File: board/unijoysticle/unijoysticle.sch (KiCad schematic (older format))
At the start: 14 parts, among them IC1 7405, IC2 7405, J1 DB9_Female, J2 DB9_Female, J3 Barrel_Jack, SW1 SW_Push, SW2 SW_SPST

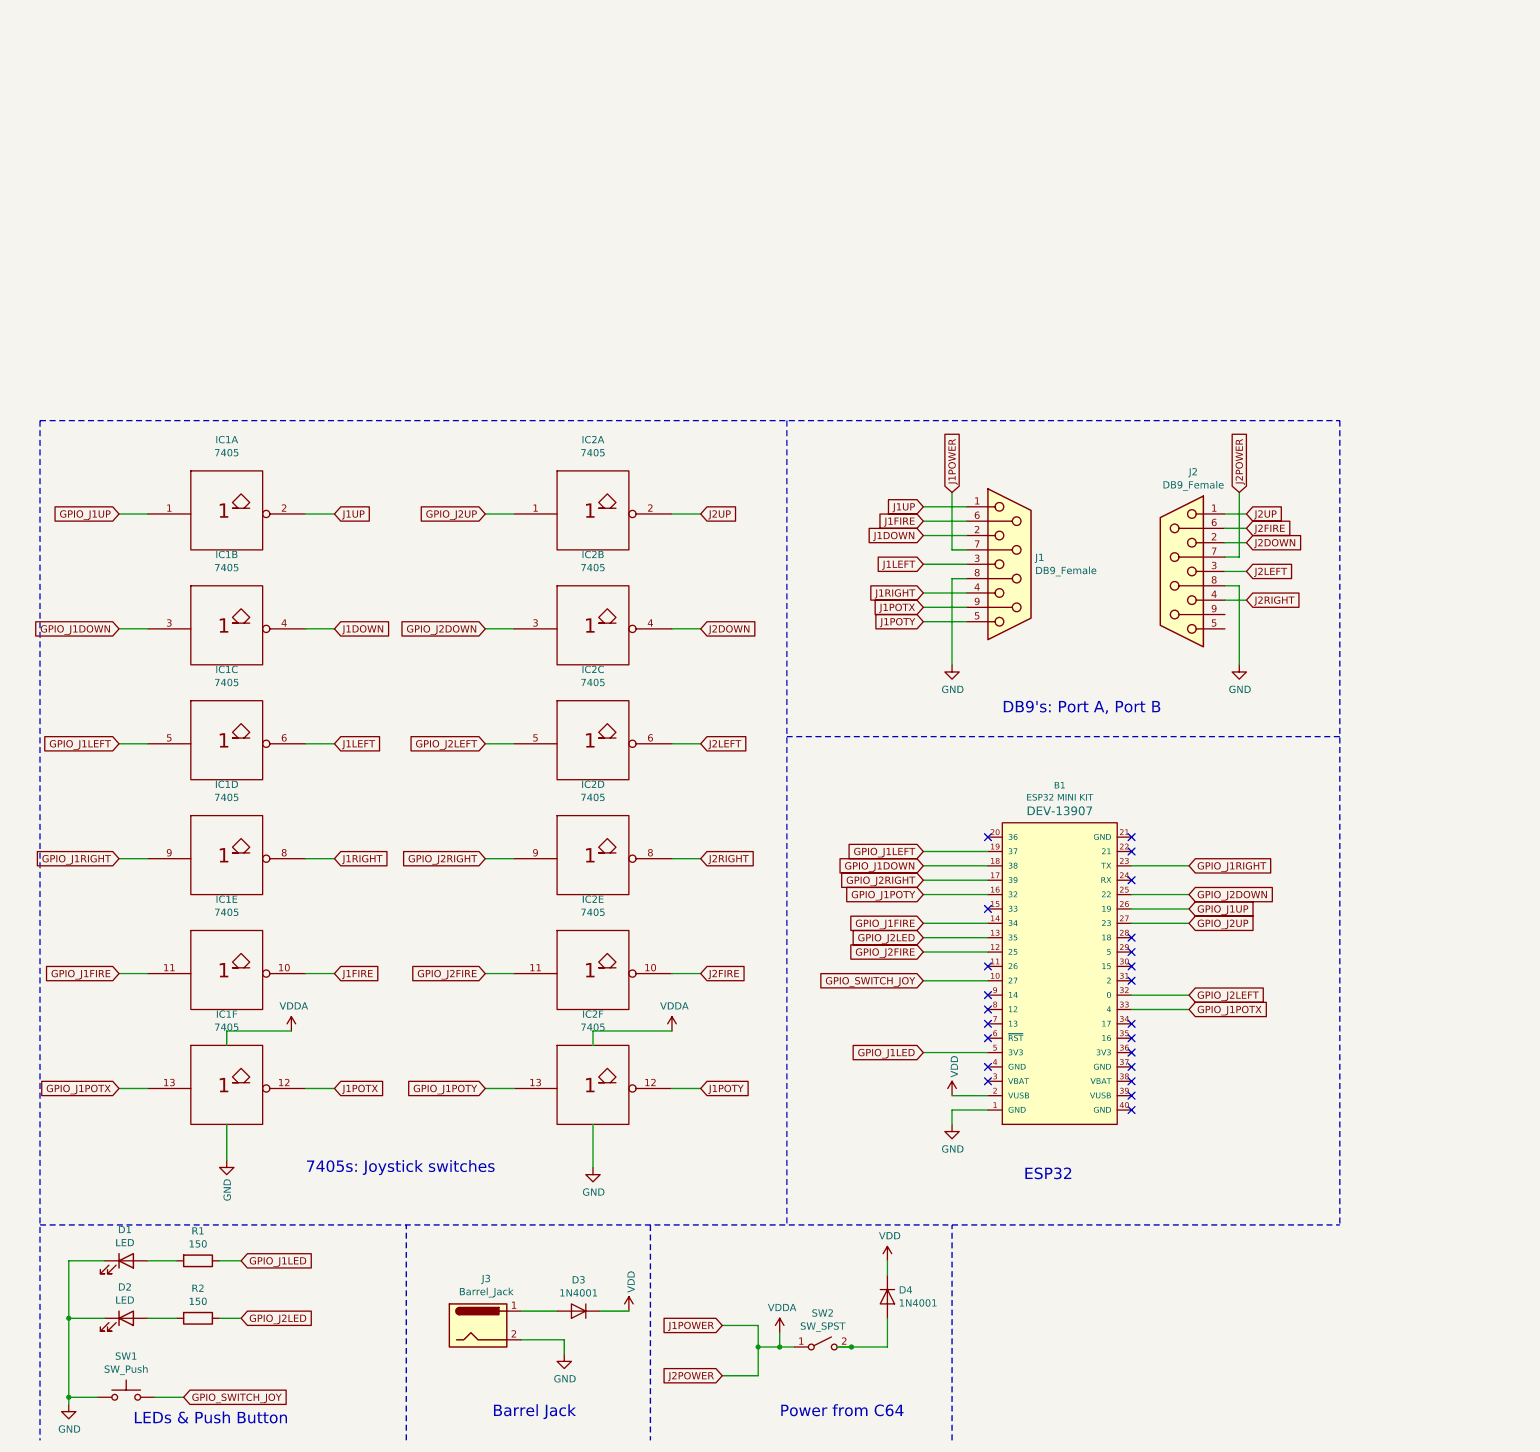
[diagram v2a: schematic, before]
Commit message: layout / schematic: replaced 7405 model with one with comes with pwr/gnd
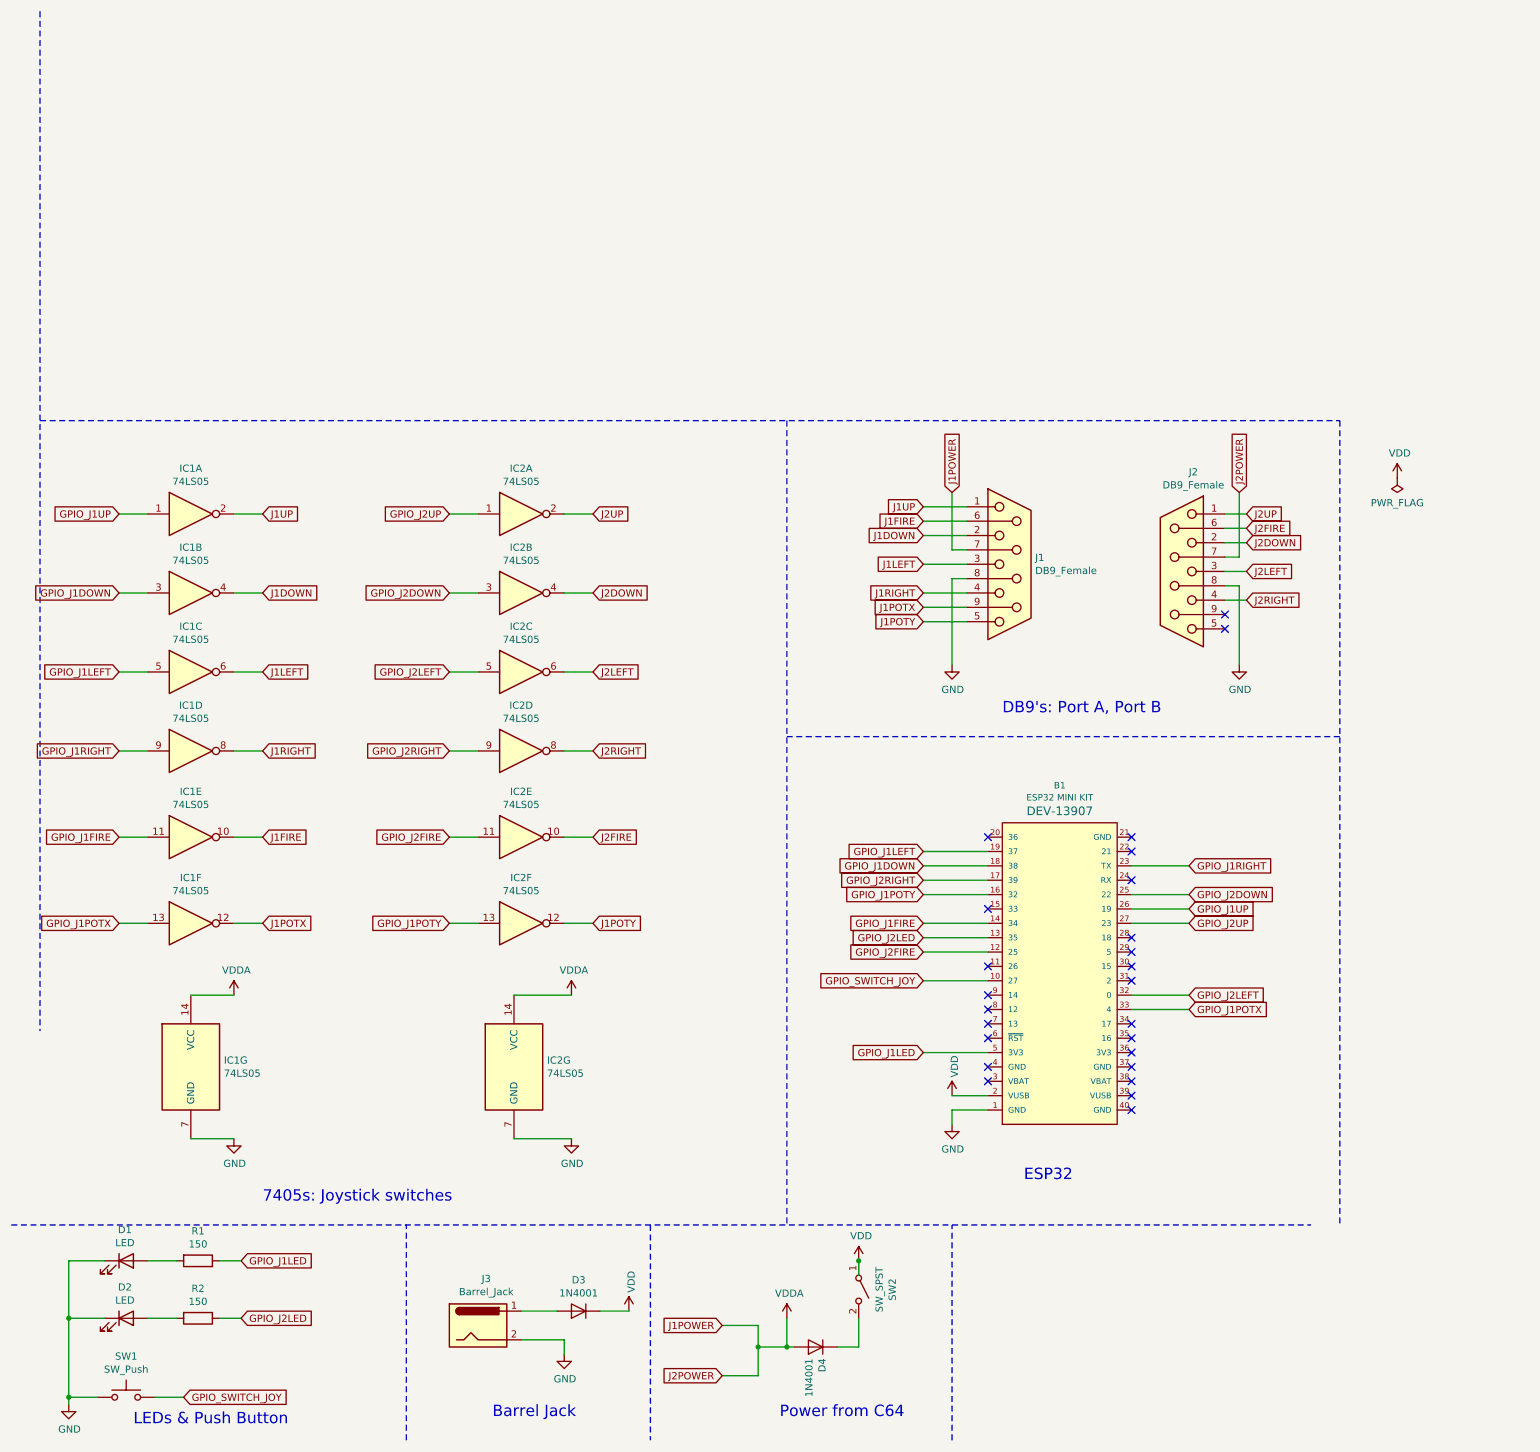
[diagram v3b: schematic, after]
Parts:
- removed IC1, IC2: 7405, Package_DIP:DIP-14_W7.62mm_LongPads, symbol 74xx_IEEE:7405
- added IC1, IC2: 74LS05, Package_DIP:DIP-14_W7.62mm_Socket_LongPads, symbol 74xx:74LS05
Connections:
- net GND: now also IC1.7 (GND), IC2.7 (GND)
- net GPIO_J1DOWN: now also IC1.3
- net GPIO_J1FIRE: now also IC1.11
- net GPIO_J1LEFT: now also IC1.5
- net GPIO_J1POTX: now also IC1.13
- net GPIO_J1POTY: now also IC2.13
- net GPIO_J1RIGHT: now also IC1.9
- net GPIO_J1UP: now also IC1.1
- net GPIO_J2DOWN: now also IC2.3
- net GPIO_J2FIRE: now also IC2.11
- net GPIO_J2LEFT: now also IC2.5
- net GPIO_J2RIGHT: now also IC2.9
- net GPIO_J2UP: now also IC2.1
- net J1DOWN: now also IC1.4
- net J1FIRE: now also IC1.10
- net J1LEFT: now also IC1.6
- net J1POTX: now also IC1.12
- net J1POTY: now also IC2.12
- net J1RIGHT: now also IC1.8
- net J1UP: now also IC1.2
- net J2DOWN: now also IC2.4
- net J2FIRE: now also IC2.10
- net J2LEFT: now also IC2.6
- net J2RIGHT: now also IC2.8
- net J2UP: now also IC2.2
- net VDD: now also SW2.1 (A); no longer D4.1 (K)
- net VDDA: now also D4.2 (A), IC1.14 (VCC), IC2.14 (VCC); no longer SW2.1 (A)
- net at SW2.2 (B): now also D4.1 (K); no longer D4.2 (A)
- no-connect marks 23 -> 25
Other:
- moved on the sheet: D4, SW2

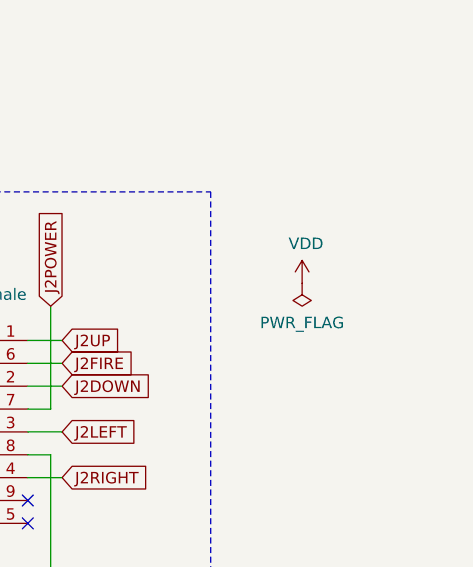
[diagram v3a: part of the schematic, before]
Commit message: board: import unijoysticle logo
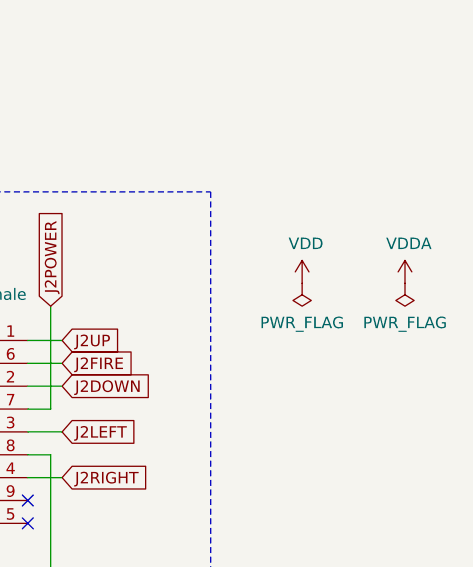
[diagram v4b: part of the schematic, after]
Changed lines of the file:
@@
 Wire Wire Line
 	1900 4700 1600 4700
+$Comp
+L power:VDDA #PWR0115
+U 1 1 5DA42FB3
+P 10450 1100
+F 0 "#PWR0115" H 10450 950 50  0001 C CNN
+F 1 "VDDA" H 10467 1273 50  0000 C CNN
+F 2 "" H 10450 1100 50  0001 C CNN
+F 3 "" H 10450 1100 50  0001 C CNN
+	1    10450 1100
+	1    0    0    -1
+$EndComp
+$Comp
+L power:PWR_FLAG #FLG0102
+U 1 1 5DA43568
+P 10450 1100
+F 0 "#FLG0102" H 10450 1175 50  0001 C CNN
+F 1 "PWR_FLAG" H 10450 1273 50  0000 C CNN
+F 2 "" H 10450 1100 50  0001 C CNN
+F 3 "~" H 10450 1100 50  0001 C CNN
+	1    10450 1100
+	-1   0    0    1
+$EndComp
 $EndSCHEMATC

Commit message: board: rev D
changes DIP switch for slide switch since it supports more amperage
board a tiny bit wider
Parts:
- SW2: footprint Button_Switch_THT:SW_DIP_SPSTx01_Slide_6.7x4.1mm_W7.62mm_P2.54mm_LowProfile -> Switches:SWITCH_SPDT_PTH_11.6X4.0MM
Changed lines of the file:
@@
 Sheet 1 1
 Title "Unijoysticle 2"
-Date "2019-09-21"
-Rev "C"
+Date "2019-09-27"
+Rev "D"
 Comp "Retro Moe"
 Comment1 "Ricardo Quesada"
@@
 F 0 "SW2" H 6250 6985 50  0000 C CNN
 F 1 "SW_SPST" H 6250 6894 50  0000 C CNN
-F 2 "Button_Switch_THT:SW_DIP_SPSTx01_Slide_6.7x4.1mm_W7.62mm_P2.54mm_LowProfile" H 6250 6750 50  0001 C CNN
+F 2 "Switches:SWITCH_SPDT_PTH_11.6X4.0MM" H 6250 6750 50  0001 C CNN
 F 3 "~" H 6250 6750 50  0001 C CNN
 	1    6250 6750

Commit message: board: rev. D
replaces the DIP switch with a slide switch, right angled.
Allows better amperage, and easier to solder.
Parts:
- SW2: footprint Switches:SWITCH_SPDT_PTH_11.6X4.0MM -> Button_Switch_THT:SW_CuK_OS102011MA1QN1_SPDT_Angled
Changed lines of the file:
@@
 F 0 "SW2" H 6250 6985 50  0000 C CNN
 F 1 "SW_SPST" H 6250 6894 50  0000 C CNN
-F 2 "Switches:SWITCH_SPDT_PTH_11.6X4.0MM" H 6250 6750 50  0001 C CNN
+F 2 "Button_Switch_THT:SW_CuK_OS102011MA1QN1_SPDT_Angled" H 6250 6750 50  0001 C CNN
 F 3 "~" H 6250 6750 50  0001 C CNN
 	1    6250 6750
